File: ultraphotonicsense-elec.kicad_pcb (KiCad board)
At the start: 2 copper layers, 83 x 38 mm, 79 parts, among them J1 Conn_Debug, J10 Conn_01x04, J11 Conn_01x04, J12 Conn_01x04, J13 Conn_01x04, J2 Conn_01x05, J3 Conn_01x05, J4 Conn_01x05, J5 Conn_01x05, J6 Conn_01x05, J7 Conn_01x05, J8 Conn_01x05, J9 Conn_01x05, P1 CAN_conn, P2 CAN_conn, Q1 BSS138, Q2 BSS138, Q3 BSS138, Q4 BSS138, Q5 BSS138, U1 TXB0108PW, U2 74HC164, U3 TCAN332, U4 LD1117S50TR_SOT223, U5 LD1117S33TR_SOT223, U6 LP38693MP-ADJ, U7 STM32F303K8Tx, Y1 Crystal

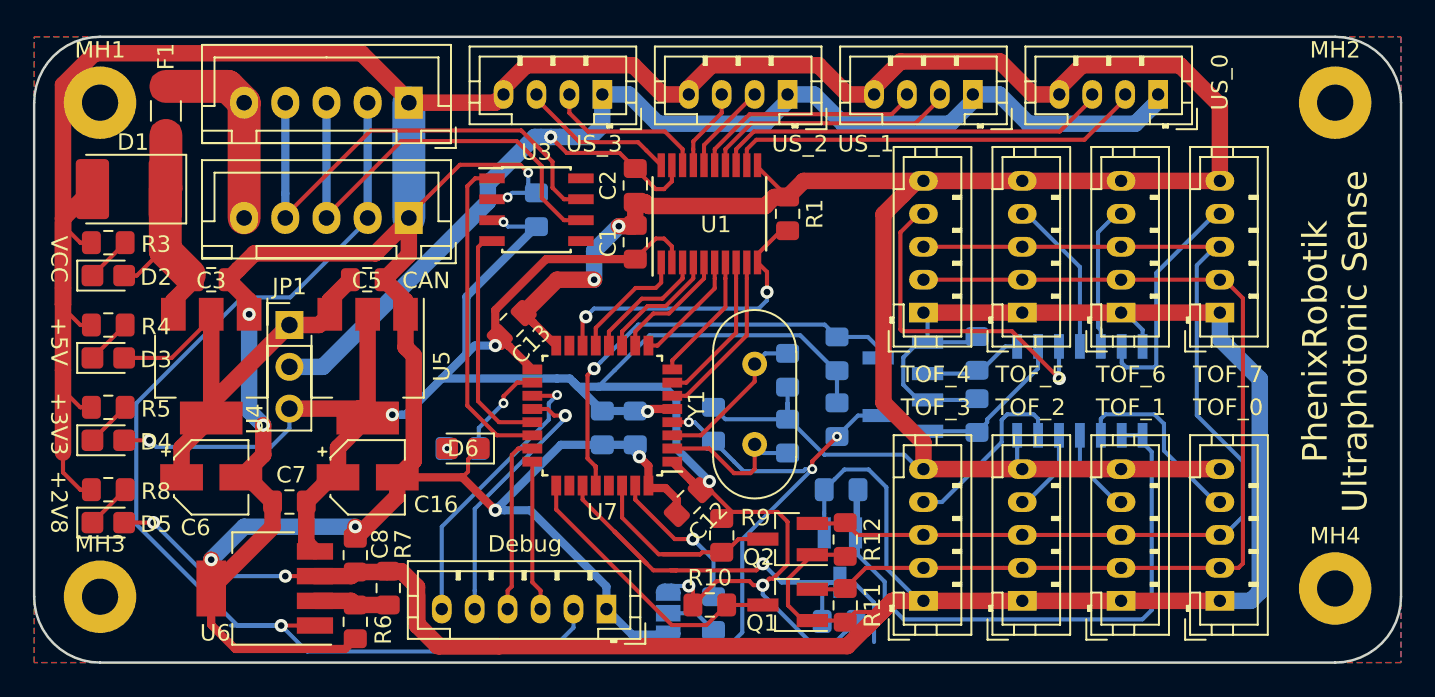
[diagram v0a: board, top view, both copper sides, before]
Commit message: update from schema
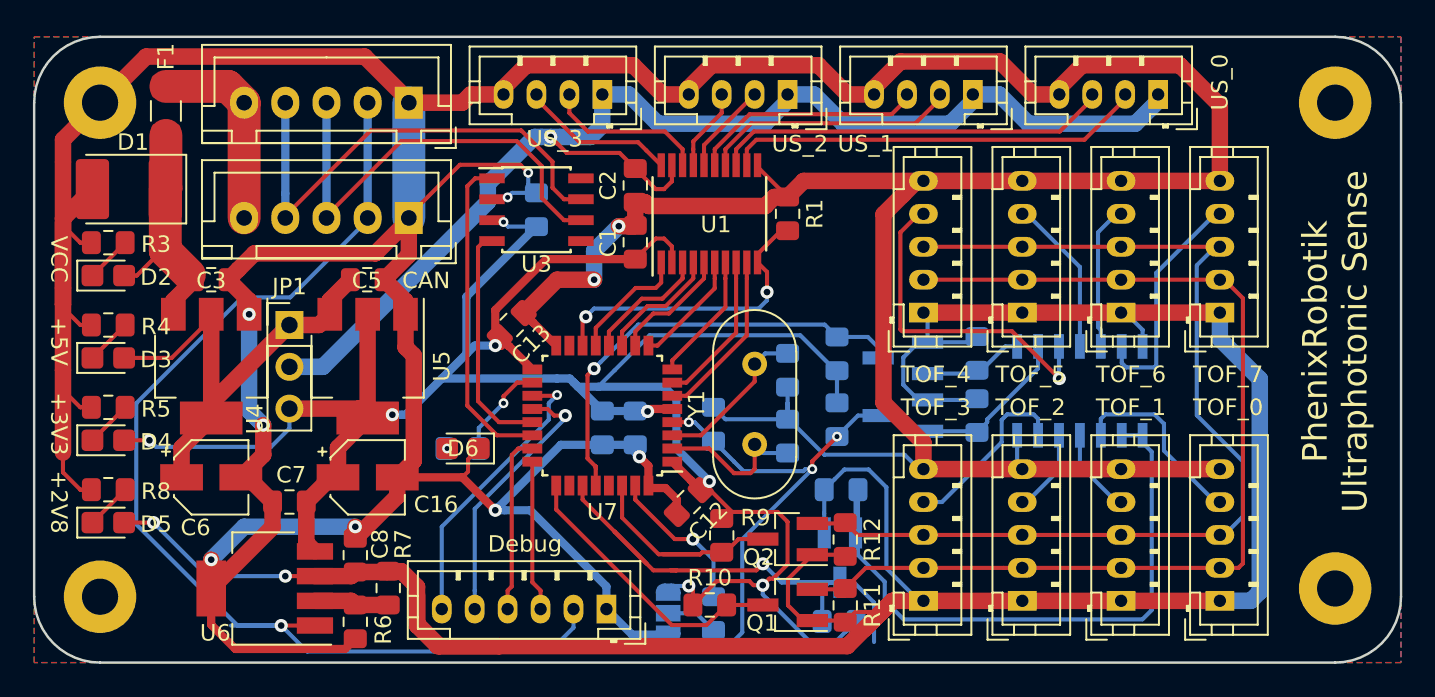
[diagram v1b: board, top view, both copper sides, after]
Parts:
- removed #LOGO1: Logo_16,9mm, PhoenixRobotik:Logo_16,9mm
- removed #LOGO3: KiCad-Logo2_6mm_SilkScreen, Symbol:KiCad-Logo2_6mm_SilkScreen
- added LOGO1: Logo_Open_Hardware_Small, PhenixRobotik:Logo_16,9mm, B.Cu at (76.8, 50.0)
- added LOGO3: Logo_Open_Hardware_Small, Symbol:KiCad-Logo_6mm_SilkScreen, B.Cu at (51.4, 65.0)
- LOGO2: renamed from #LOGO2; value OSHW-Logo2_7.3x6mm_SilkScreen -> Logo_Open_Hardware_Small
- moved LOGO2 22.0 mm to (42.8, 55.4)
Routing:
- net GND: track 380.7 -> 378.5 mm
